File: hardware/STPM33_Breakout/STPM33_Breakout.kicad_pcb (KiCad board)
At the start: 2 copper layers, 55 x 40 mm, 5 parts, among them U1 STPM33

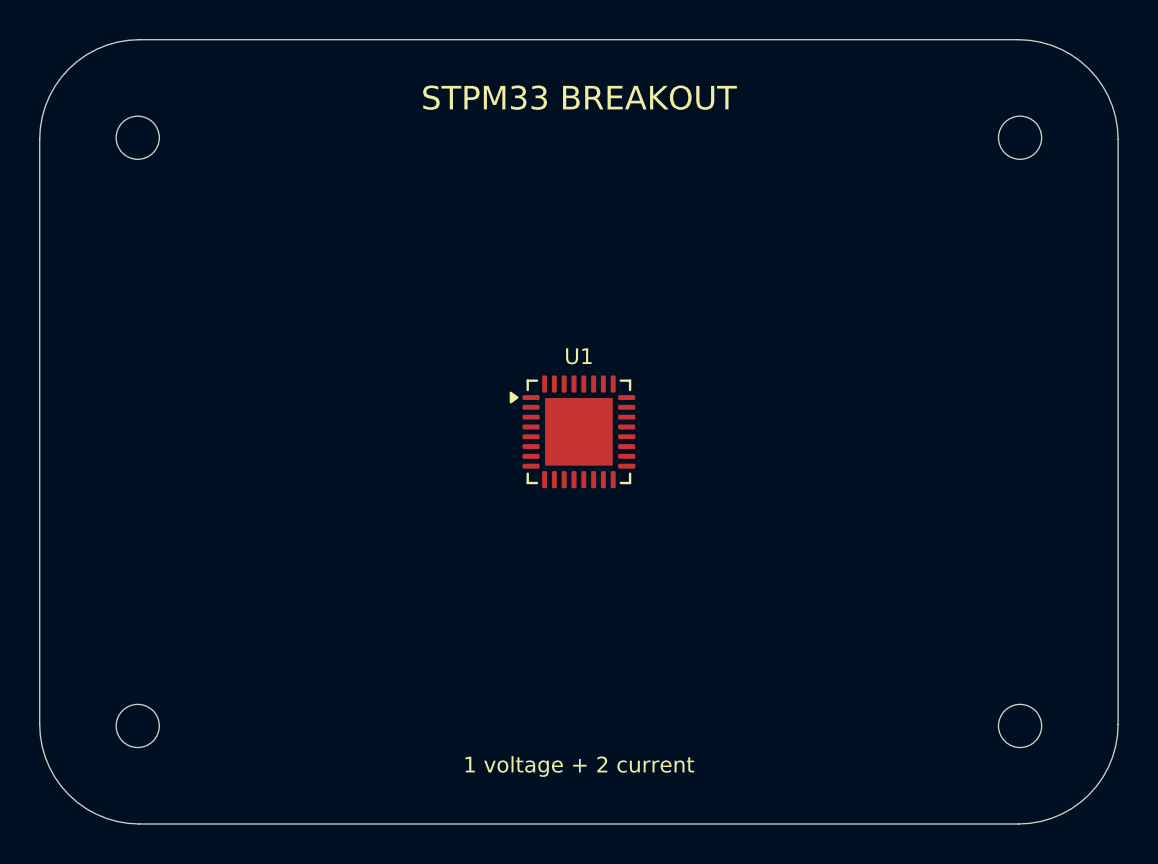
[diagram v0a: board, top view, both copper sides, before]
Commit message: Build production STPM33 breakout
Implement the dual-current isolated-voltage schematic, routed PCB, sourcing metadata, project-local assets, renders, and ERC/DRC-gated Elecrow fabrication package. Document the SPI/UART selector and reproducible KiCad 10 workflow.

Co-authored-by: Copilot <223556219+Copilot@users.noreply.github.com>
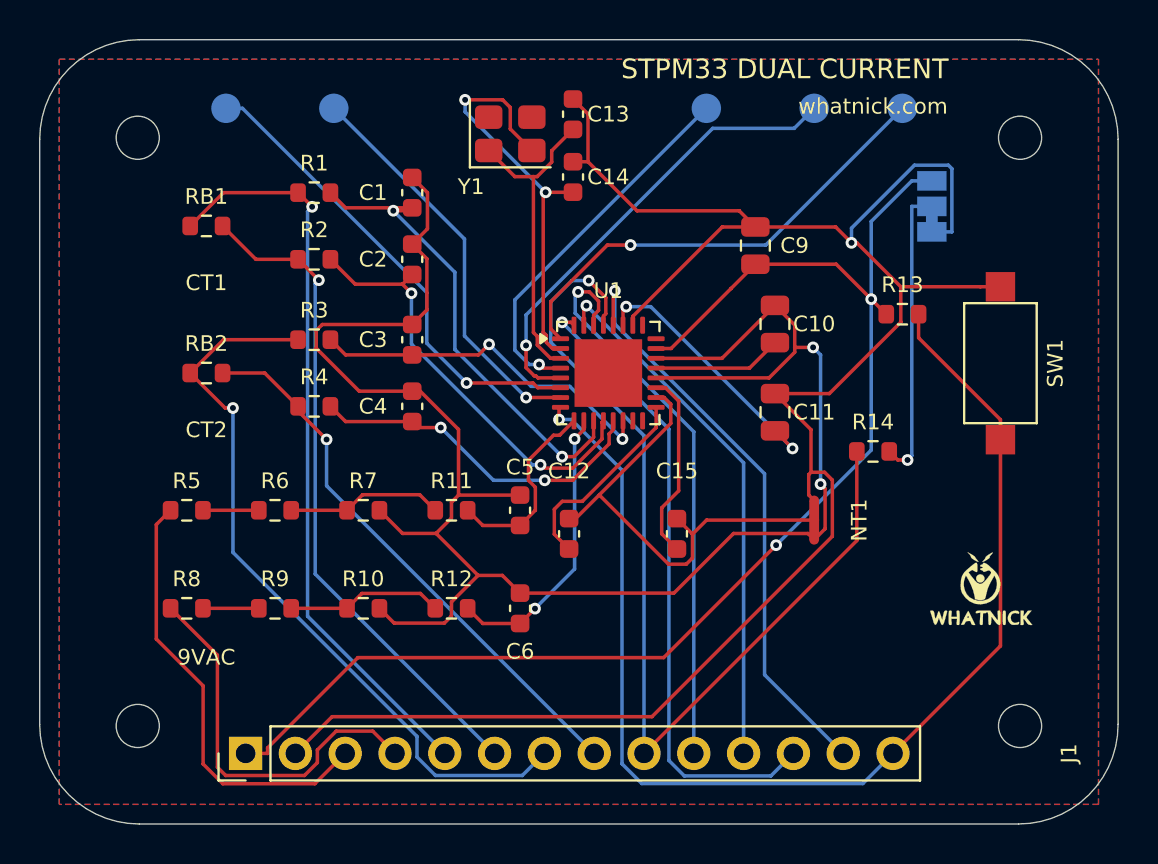
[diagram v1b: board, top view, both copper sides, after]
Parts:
- added C1: 330n, C_0603_1608Metric, F.Cu at (39.0, 27.8)
- added C10: 1u, C_0805_2012Metric, F.Cu at (57.5, 34.5)
- added C11: 4.7u, C_0805_2012Metric, F.Cu at (57.5, 39.0)
- added C12: 100n, C_0603_1608Metric, F.Cu at (47.0, 45.2)
- added C13: 15p, C_0603_1608Metric, F.Cu at (47.2, 23.8)
- added C14: 15p, C_0603_1608Metric, F.Cu at (47.2, 27.0)
- added C15: 100n, C_0603_1608Metric, F.Cu at (52.5, 45.2)
- added C2: 330n, C_0603_1608Metric, F.Cu at (39.0, 31.2)
- added C3: 330n, C_0603_1608Metric, F.Cu at (39.0, 35.3)
- added C4: 330n, C_0603_1608Metric, F.Cu at (39.0, 38.7)
- added C5: 33n, C_0603_1608Metric, F.Cu at (44.5, 44.0)
- added C6: 33n, C_0603_1608Metric, F.Cu at (44.5, 49.0)
- added C9: 1u, C_0805_2012Metric, F.Cu at (56.5, 30.5)
- added J1: BREADBOARD I/O, PinHeader_1x14_P2.54mm_Vertical, F.Cu at (30.5, 56.4)
- added LOGO_OSHW: OSHW_Logo, OSHW_Logo, B.Cu at (66.0, 51.0)
- added LOGO_W: Whatnick_Logo, Whatnick_Logo, F.Cu at (68.0, 48.0)
- added NT1: ANALOG/DIGITAL STAR, NetTie-3_SMD_Pad0.5mm, F.Cu at (59.5, 44.5)
- added R1: 100R, R_0603_1608Metric, F.Cu at (34.0, 27.8)
- added R10: 2.49k, R_0603_1608Metric, F.Cu at (36.5, 49.0)
- added R11: 1k, R_0603_1608Metric, F.Cu at (41.0, 44.0)
- added R12: 1k, R_0603_1608Metric, F.Cu at (41.0, 49.0)
- added R13: 10k, R_0603_1608Metric, F.Cu at (64.0, 34.0)
- added R14: 10k, R_0603_1608Metric, F.Cu at (62.5, 41.0)
- added R2: 100R, R_0603_1608Metric, F.Cu at (34.0, 31.2)
- added R3: 100R, R_0603_1608Metric, F.Cu at (34.0, 35.3)
- added R4: 100R, R_0603_1608Metric, F.Cu at (34.0, 38.7)
- added R5: 100k, R_0603_1608Metric, F.Cu at (27.5, 44.0)
- added R6: 100k, R_0603_1608Metric, F.Cu at (32.0, 44.0)
- added R7: 2.49k, R_0603_1608Metric, F.Cu at (36.5, 44.0)
- added R8: 100k, R_0603_1608Metric, F.Cu at (27.5, 49.0)
- added R9: 100k, R_0603_1608Metric, F.Cu at (32.0, 49.0)
- added RB1: 2.4R, R_0603_1608Metric, F.Cu at (28.5, 29.5)
- added RB2: 2.4R, R_0603_1608Metric, F.Cu at (28.5, 37.0)
- added SJ1: SPI / UART, SolderJumper-3_P1.3mm_Bridged12_Pad1.0x1.5mm, B.Cu at (65.5, 28.5)
- added SW1: RESET, SW_SPST_CK_RS282G05A3, F.Cu at (69.0, 36.5)
- added TP1: INT1, TestPoint_Pad_D1.5mm, B.Cu at (29.5, 23.5)
- added TP2: INT2, TestPoint_Pad_D1.5mm, B.Cu at (35.0, 23.5)
- added TP3: LED1, TestPoint_Pad_D1.5mm, B.Cu at (54.0, 23.5)
- added TP4: LED2, TestPoint_Pad_D1.5mm, B.Cu at (59.5, 23.5)
- added TP5: CLKOUT_ZCR, TestPoint_Pad_D1.5mm, B.Cu at (64.0, 23.5)
- added Y1: 16MHz, Crystal_SMD_3225-4Pin_3.2x2.5mm, F.Cu at (44.0, 24.8)
- H1, H2, H3, H4: value M2 -> MountingHole_2.2mm_M2
- moved U1 3.35 mm to (49.0, 37.0)
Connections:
- U1 pad 1: (no net) -> CLKOUT_ZCR
- U1 pad 10: (no net) -> VIN1
- U1 pad 11: (no net) -> IIP1
- U1 pad 12: (no net) -> IIN1
- U1 pad 13: (no net) -> IIN2
- U1 pad 14: (no net) -> IIP2
- U1 pad 15: (no net) -> unconnected-(U1-NC1-Pad15)
- U1 pad 16: (no net) -> unconnected-(U1-NC2-Pad16)
- U1 pad 17: (no net) -> VREF1
- U1 pad 18: (no net) -> GND_REF
- U1 pad 19: (no net) -> VREF2
- U1 pad 2: (no net) -> XTAL2
- U1 pad 20: (no net) -> GNDA
- U1 pad 21: (no net) -> VDDA
- U1 pad 22: (no net) -> GNDA
- U1 pad 23: (no net) -> +3V3
- U1 pad 24: (no net) -> unconnected-(U1-NC3-Pad24)
- U1 pad 25: (no net) -> unconnected-(U1-NC4-Pad25)
- U1 pad 26: (no net) -> DGND
- U1 pad 27: (no net) -> VDDD
- U1 pad 28: (no net) -> SYN
- U1 pad 29: (no net) -> SCS
- U1 pad 3: (no net) -> XTAL1
- U1 pad 30: (no net) -> SCL
- U1 pad 31: (no net) -> MOSI_RXD
- U1 pad 32: (no net) -> MISO_TXD
- U1 pad 4: (no net) -> LED1
- U1 pad 5: (no net) -> LED2
- U1 pad 6: (no net) -> INT1
- U1 pad 7: (no net) -> INT2
- U1 pad 8: (no net) -> EN
- U1 pad 9: (no net) -> VIP1
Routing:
- net DGND: track 0.00 -> 100.3 mm, vias 0 -> 1
- net GNDA: track 0.00 -> 93.5 mm, vias 0 -> 2
- net +3V3: track 0.00 -> 68.7 mm, vias 0 -> 2
- net EN: track 0.00 -> 61.2 mm, vias 0 -> 1
- net SCS: track 0.00 -> 50.0 mm, vias 0 -> 1
- net CT2_P: track 0.00 -> 38.2 mm, vias 0 -> 1
- net CT1_P: track 0.00 -> 38.1 mm, vias 0 -> 1
- net CT1_N: track 0.00 -> 34.1 mm, vias 0 -> 1
- net MISO_TXD: track 0.00 -> 32.4 mm, vias 0 -> 1
- net SYN: track 0.00 -> 30.2 mm, vias 0 -> 1
- net SCL: track 0.00 -> 28.7 mm, vias 0 -> 1
- net CT2_N: track 0.00 -> 28.5 mm, vias 0 -> 1
- net MOSI_RXD: track 0.00 -> 27.2 mm, vias 0 -> 1
- net IIP1: track 0.00 -> 24.5 mm, vias 0 -> 2
- net INT1: track 0.00 -> 24.5 mm, vias 0 -> 1
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- added copper zone on B.Cu, net DGND
- added copper zone on F.Cu, net GNDA
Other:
- board text added: "3V3"
- board text added: "9VAC"
- board text added: "CLK/ZCR"
- board text added: "CT1"
- board text added: "CT1+"
- board text added: "CT1-"
- board text added: "CT2"
- board text added: "CT2+"
- board text added: "CT2-"
- board text added: "EN"
- board text added: "GND"
- board text added: "INT1"
- board text added: "INT2"
- board text added: "ISOLATED 9VAC + CT INPUTS ONLY"
- board text added: "LED1"
- board text added: "LED2"
- board text added: "MISO"
- board text added: "MOSI"
- board text added: "NOT FOR DIRECT MAINS"
- board text added: "SCL"
- board text added: "SCS"
- board text added: "SPI"
- board text added: "STPM33 DUAL CURRENT"
- board text added: "SYN"
- board text added: "TAPR OHL 1.0"
- board text added: "UART"
- board text added: "VAC+"
- board text added: "VAC-"
- board text added: "v1.0 2026-10-06"
- board text added: "whatnick.com"
- board text removed: "1 voltage + 2 current"
- board text removed: "ANALOG INPUT / FILTER ZONE"
- board text removed: "POWER / DIGITAL I/O ZONE"
- board text removed: "STPM33 BREAKOUT"
- board text removed: "whatnick.com | TAPR OHL | NOT ISOLATED"
